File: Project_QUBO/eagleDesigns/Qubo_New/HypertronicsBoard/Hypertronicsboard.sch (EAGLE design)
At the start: 21 parts

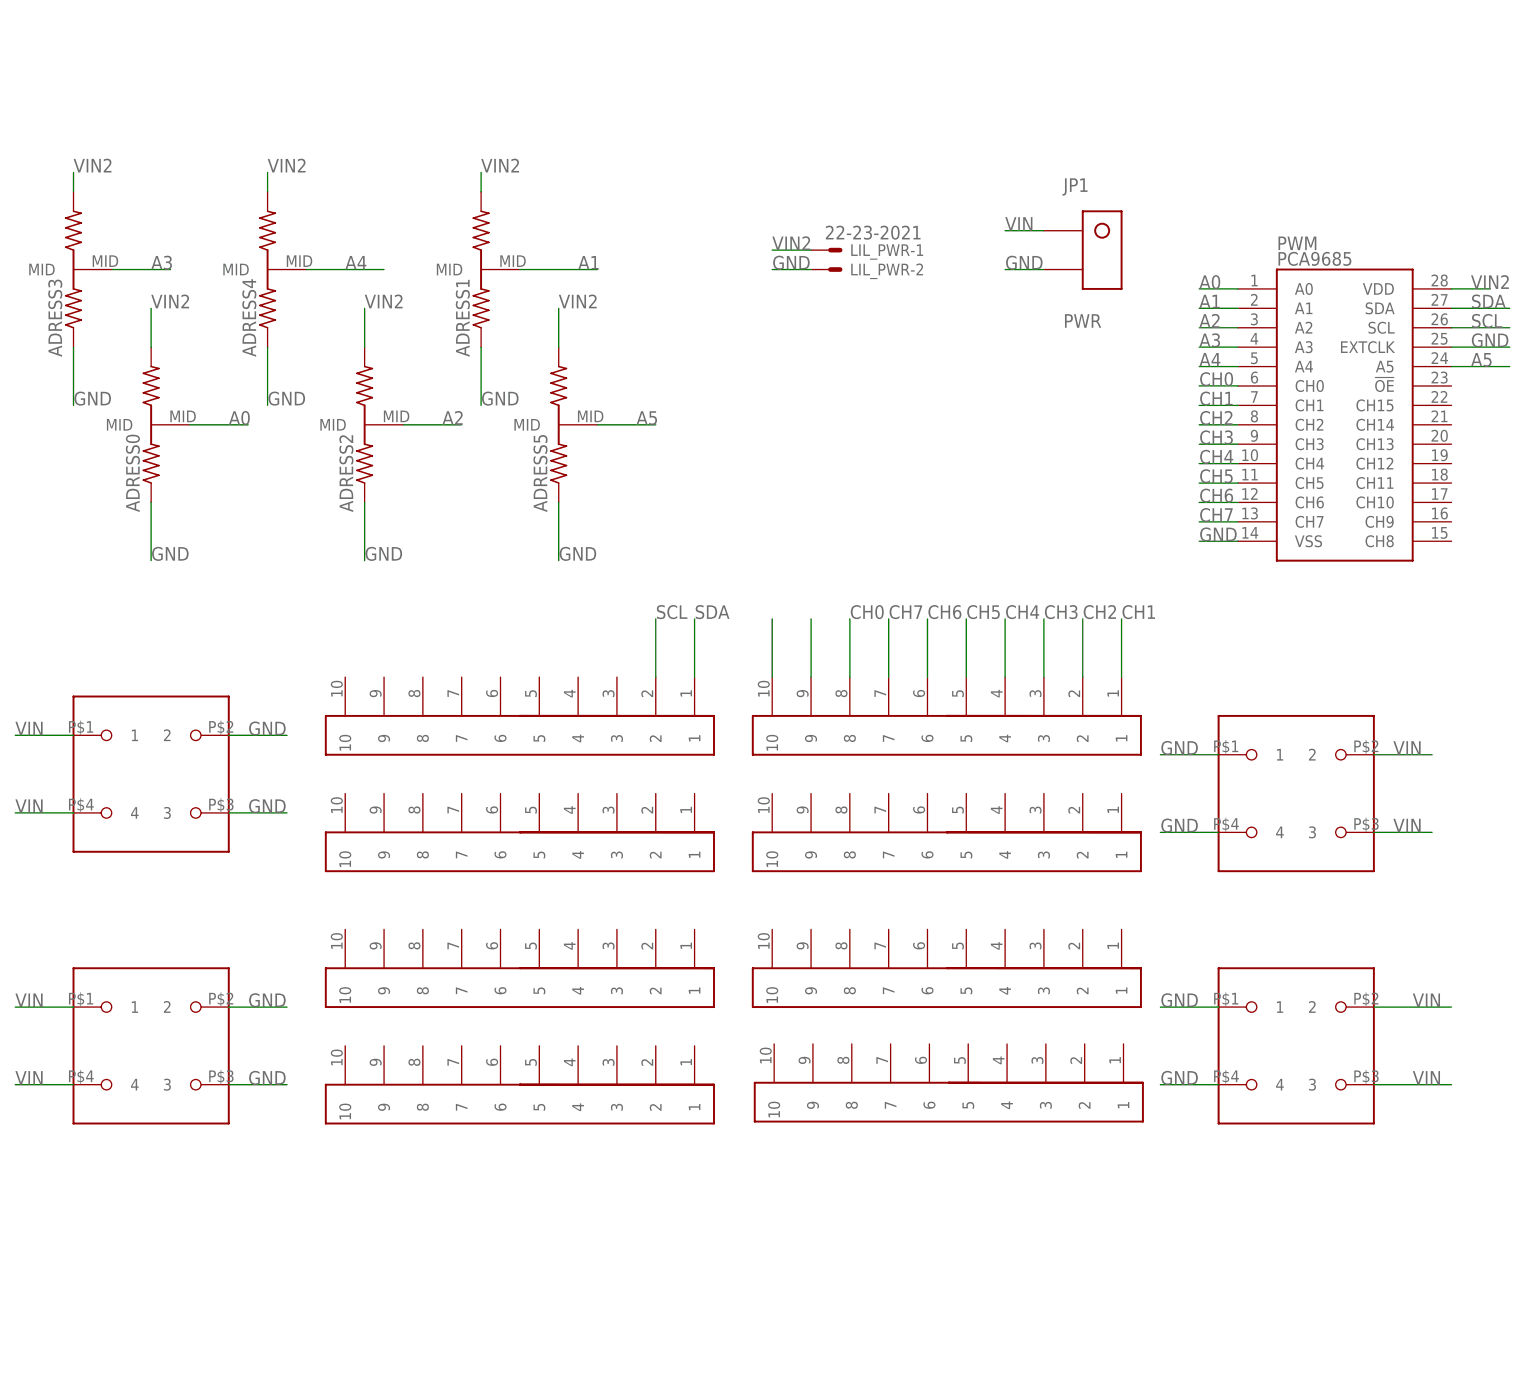
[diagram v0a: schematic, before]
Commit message: created HyperArmboard
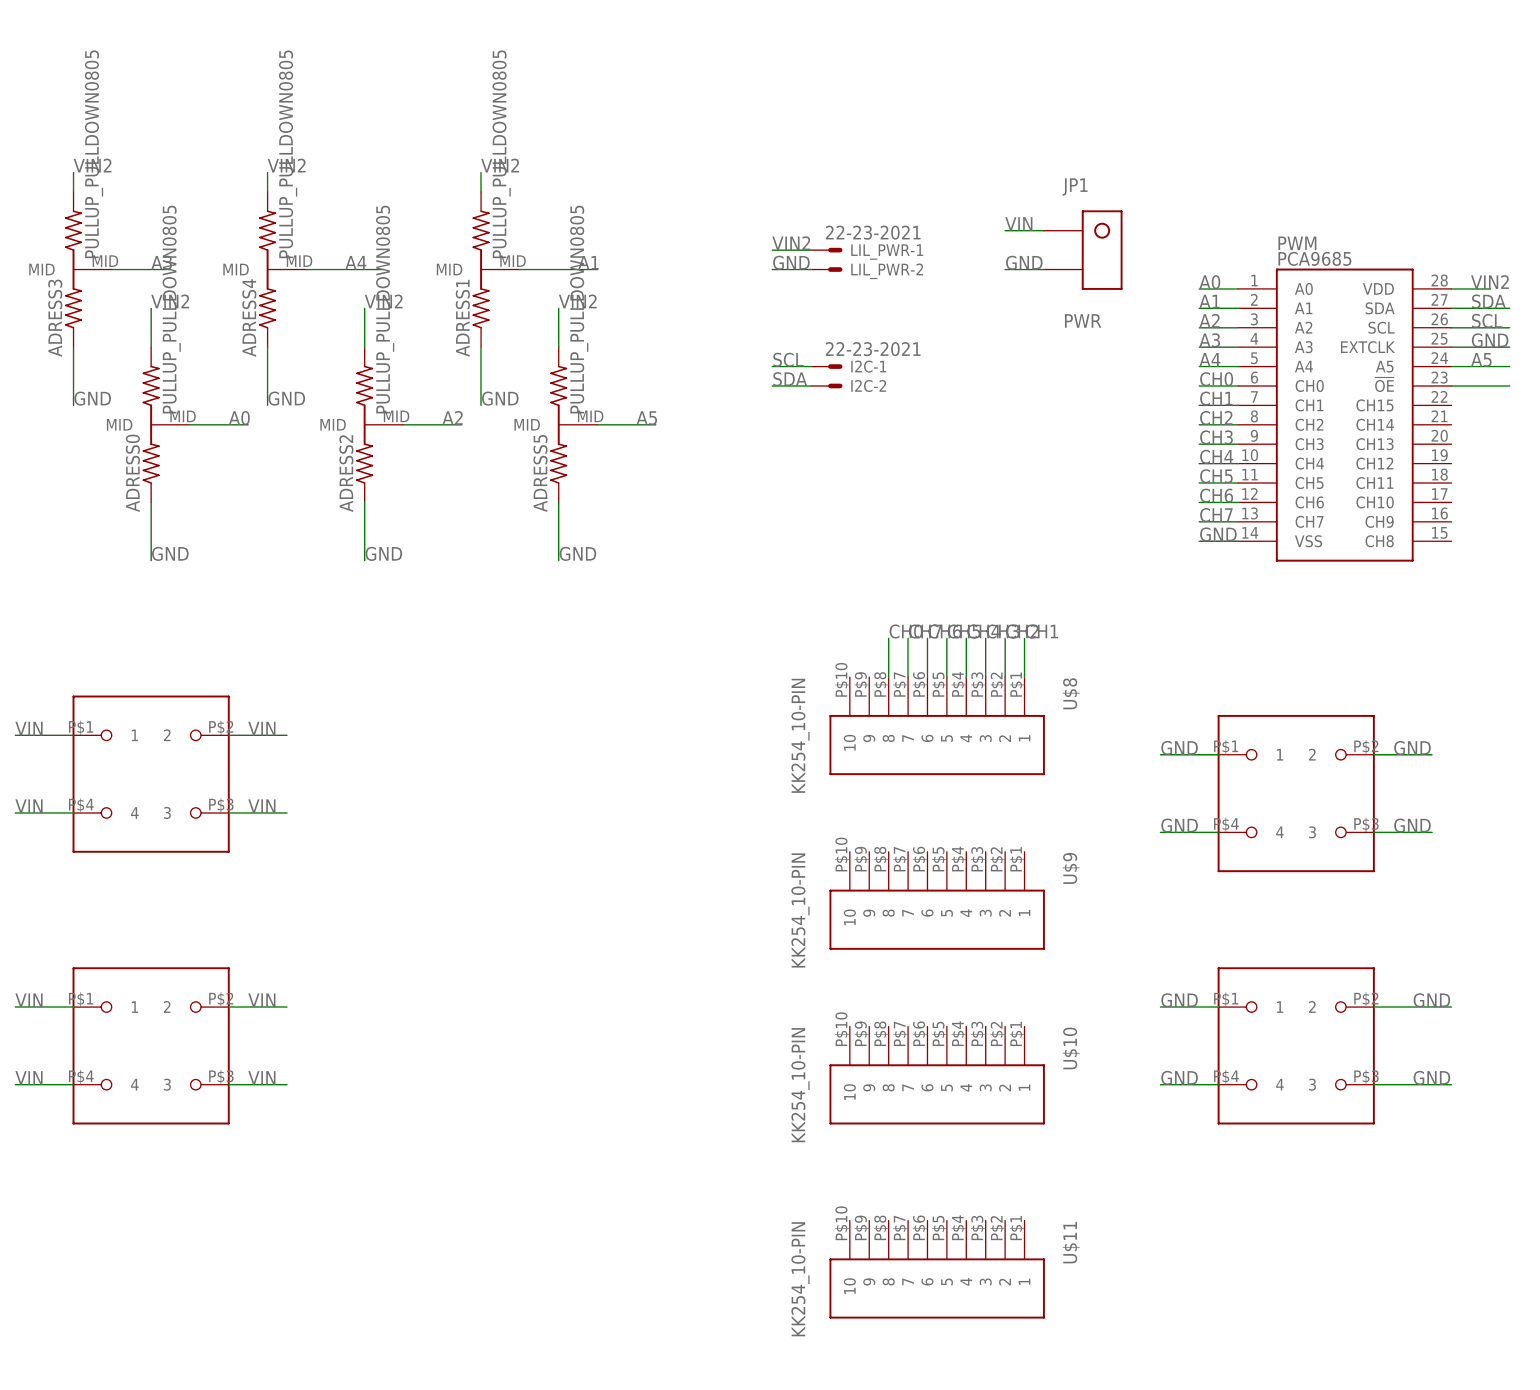
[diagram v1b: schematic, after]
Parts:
- removed U$12, U$5, U$6, U$7: CONN-RECEPT-2MM-VERT-AU-10POS, samtec:CONN-RECEPT-2MM-VERT-AU-10POS
- added I2C: 22-23-2021, con-molex_MOD:22-23-2021
- U$10, U$11, U$8, U$9: value CONN-RECEPT-2MM-VERT-AU-10POS -> KK254_10-PIN; device samtec:CONN-RECEPT-2MM-VERT-AU-10POS -> molex:KK254_10-PIN
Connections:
- removed net N$10: U$10.10
- removed net N$9: U$10.9
- new net N$1: PWM.!OE
- net CH0: now also U$8.8; no longer U$10.8
- net CH1: now also U$8.1; no longer U$10.1
- net CH2: now also U$8.2; no longer U$10.2
- net CH3: now also U$8.3; no longer U$10.3
- net CH4: now also U$8.4; no longer U$10.4
- net CH5: now also U$8.5; no longer U$10.5
- net CH6: now also U$8.6; no longer U$10.6
- net CH7: now also U$8.7; no longer U$10.7
- net GND: now also U$3.2, U$3.3, U$4.2, U$4.3; no longer U$1.2, U$1.3, U$2.2, U$2.3
- net SCL: now also I2C-1.S; no longer U$5.2
- net SDA: now also I2C-2.S; no longer U$5.1
- net VIN: now also U$1.2, U$1.3, U$2.2, U$2.3; no longer U$3.2, U$3.3, U$4.2, U$4.3
